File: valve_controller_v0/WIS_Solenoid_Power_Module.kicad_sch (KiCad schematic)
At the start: 22 parts, among them J3 Solenoid_connector, SW1 SW_DIP_x02, U1 DRV8231ADSGR, U2 DRV8231ADSGR, U3 LMR62421XMF, U4 LT218

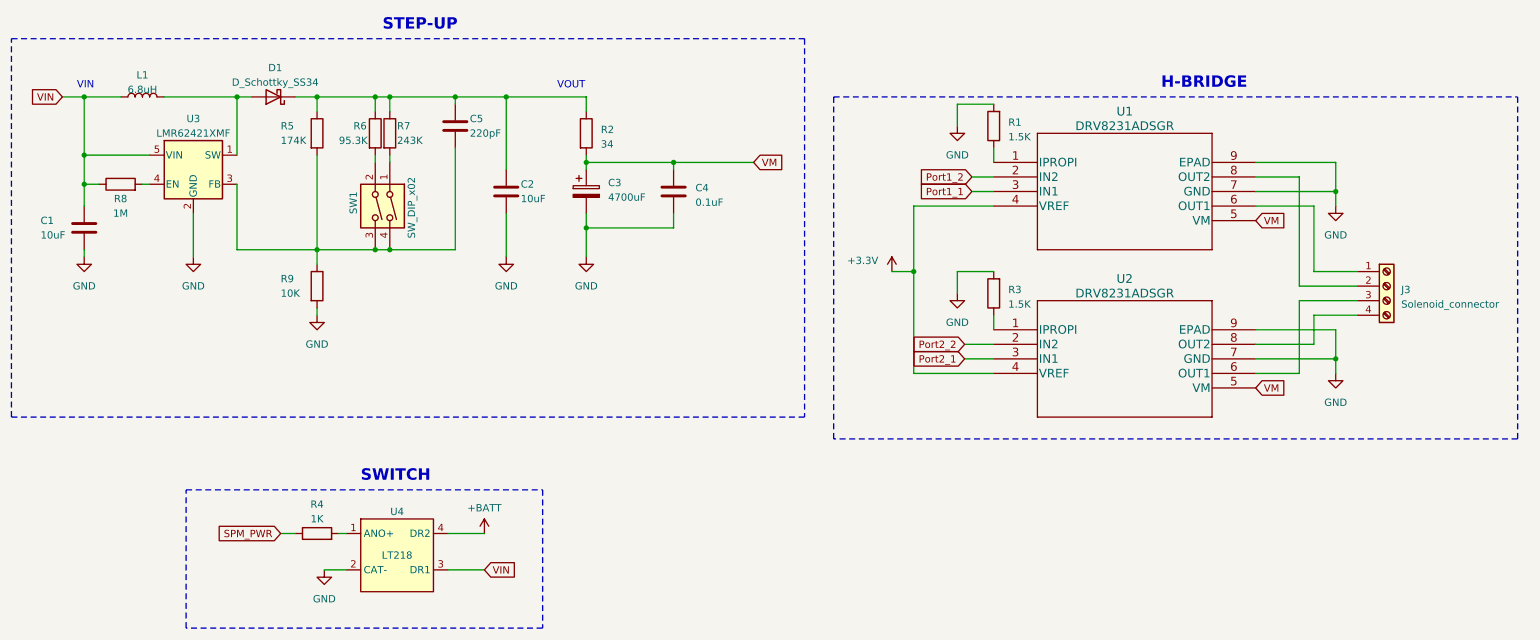
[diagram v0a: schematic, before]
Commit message: Replaced battery charger and battery holder
- Replaced battery charger to support the  new solar panel
- Replaced the battery holder by a plastic enclosure one
- Reconnected the on/off switch to avoid putting EN pin floating temporarly whne swithced
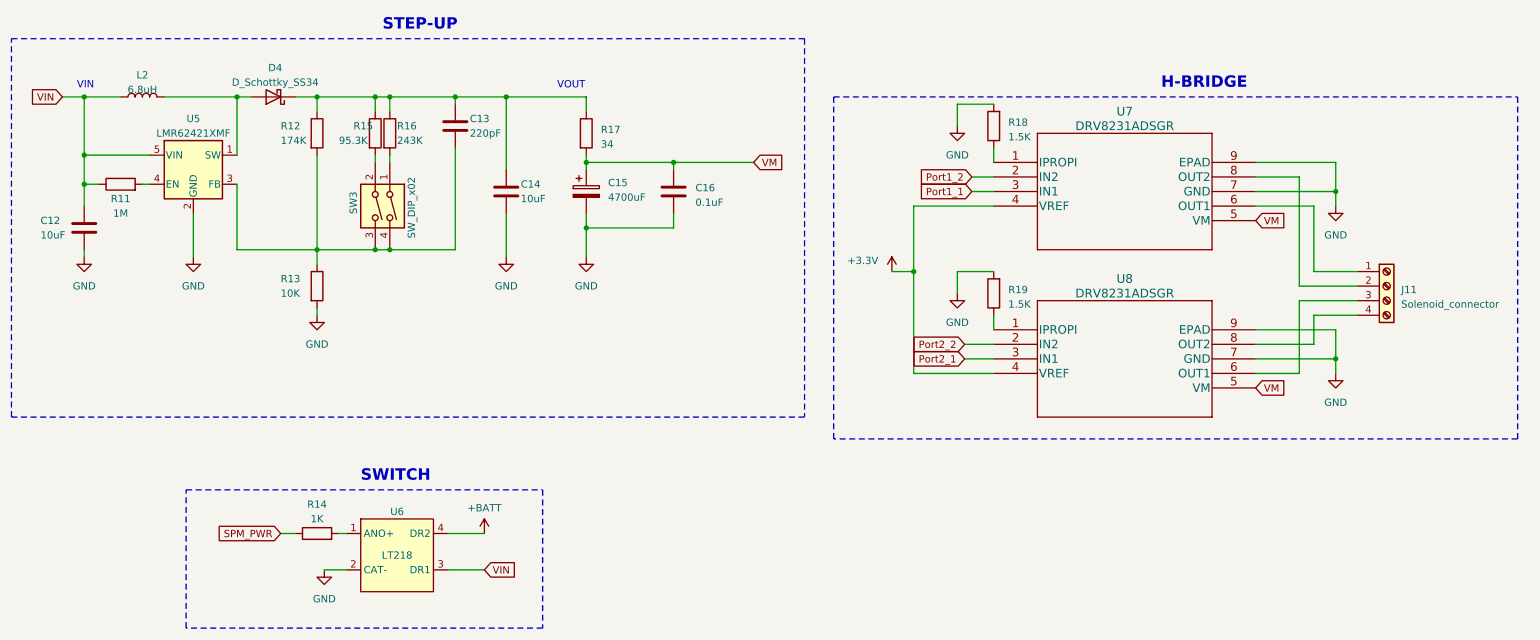
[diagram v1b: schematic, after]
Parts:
- renumbered C1 to C12, C5 to C13, C2 to C14, C3 to C15, C4 to C16, D1 to D4, J3 to J11, L1 to L2, R8 to R11, R5 to R12, R9 to R13, R4 to R14, R6 to R15, R7 to R16, R2 to R17, R1 to R18, R3 to R19, SW1 to SW3, U3 to U5, U4 to U6, U1 to U7, U2 to U8
